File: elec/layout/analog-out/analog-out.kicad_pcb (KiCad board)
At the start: 2 copper layers, 8 parts, among them U1 10kΩ ±1% 62.5mW, U2 10kΩ ±1% 62.5mW, U3 BW CMRR Ib Vos GBW Iout SR, U5 100nF ±10% 50V X7R, U6 100kΩ ±1% 62.5mW, U7 1µF ±10% 25V X5R

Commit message: Build everything with ordered params to fix frozen builds
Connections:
- D1 pad 2: gnd -> gnd-1
- U2 pad 1: gnd -> gnd-1
- U3 pad 4: gnd -> gnd-1
- U3 pad 8: hv -> hv-1
- U4 pad 1: line -> line-1
- U4 pad 2: gnd-1 -> gnd
- U4 pad 3: hv-1 -> hv
- U4 pad 4: line-1 -> line
- U4 pad 6: gnd -> gnd-1
- U5 pad 2: gnd-1 -> gnd
- U6 pad 1: line -> line-1
- U7 pad 1: hv -> hv-1
- U7 pad 2: gnd -> gnd-1
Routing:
- net gnd-1: track 0.00 -> 29.7 mm, vias 0 -> 2
- net gnd: track 29.7 -> 0.00 mm, vias 2 -> 0
- net line-1: track 0.00 -> 1.94 mm
- net line: track 1.94 -> 0.00 mm
- net hv-1: track 0.00 -> 1.56 mm
- net hv: track 1.56 -> 0.00 mm

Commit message: Cleanup layout for usb hub and usb-uart, add CM5 controller heatsink outline
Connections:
- D1 pad 2: gnd-1 -> gnd
- U2 pad 1: gnd-1 -> gnd
- U3 pad 4: gnd-1 -> gnd
- U3 pad 8: hv-1 -> hv
- U4 pad 1: line-1 -> line
- U4 pad 2: gnd -> gnd-1
- U4 pad 3: hv -> hv-1
- U4 pad 4: line -> line-1
- U4 pad 6: gnd-1 -> gnd
- U5 pad 2: gnd -> gnd-1
- U6 pad 1: line-1 -> line
- U7 pad 1: hv-1 -> hv
- U7 pad 2: gnd-1 -> gnd
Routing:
- net gnd-1: track 29.7 -> 0.00 mm, vias 2 -> 0
- net gnd: track 0.00 -> 29.7 mm, vias 0 -> 2
- net line-1: track 1.94 -> 0.00 mm
- net line: track 0.00 -> 1.94 mm
- net hv-1: track 1.56 -> 0.00 mm
- net hv: track 0.00 -> 1.56 mm
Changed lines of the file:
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@@
     )
     (net 0 "")
-    (net 1 "line")
+    (net 1 "line-1")
     (net 2 "amplifier.opamp.footprint.pins[6].net-net")
     (net 3 "amplifier.opamp.footprint.pins[5].net-net")
     (net 4 "non_inverting_input")
     (net 5 "line-2")
-    (net 6 "gnd-1")
-    (net 7 "line-1")
+    (net 6 "gnd")
+    (net 7 "line")
     (net 8 "inverting_input")
     (net 9 "amplifier.opamp.footprint.pins[4].net-net")
-    (net 10 "hv")
+    (net 10 "hv-1")
     (net 11 "output")
-    (net 12 "hv-1")
-    (net 13 "gnd")
+    (net 12 "hv")
+    (net 13 "gnd-1")
     (footprint "atopile:SMB_L4.6-W3.6-LS5.3-RD-330cb3"
         (layer "F.Cu")
@@
             (size 2.05 2.19)
             (layers "F.Cu" "F.Mask" "F.Paste")
-            (net 6 "gnd-1")
+            (net 6 "gnd")
         )
         (embedded_fonts no)
@@
             (size 0.57 0.54)
             (layers "F.Cu" "F.Mask" "F.Paste")
-            (net 7 "line-1")
+            (net 7 "line")
         )
         (pad "2" smd rect
@@
             (size 0.79 0.54)
             (layers "F.Cu" "F.Mask" "F.Paste")
-            (net 12 "hv-1")
+            (net 12 "hv")
         )
         (pad "2" smd rect
@@
             (size 0.79 0.54)
             (layers "F.Cu" "F.Mask" "F.Paste")
-            (net 6 "gnd-1")
+            (net 6 "gnd")
         )
         (embedded_fonts no)
@@
             (size 0.53 1.07)
             (layers "F.Cu" "F.Mask" "F.Paste")
-            (net 7 "line-1")
+            (net 7 "line")
         )
         (pad "2" smd rect
@@
             (size 0.53 1.07)
             (layers "F.Cu" "F.Mask" "F.Paste")
-            (net 13 "gnd")
+            (net 13 "gnd-1")
         )
         (pad "3" smd rect
@@
             (size 0.53 1.07)
             (layers "F.Cu" "F.Mask" "F.Paste")
-            (net 10 "hv")
+            (net 10 "hv-1")
         )
         (pad "4" smd rect
@@
             (size 0.53 1.07)
             (layers "F.Cu" "F.Mask" "F.Paste")
-            (net 1 "line")
+            (net 1 "line-1")
         )
         (pad "5" smd rect
@@
             (size 0.53 1.07)
             (layers "F.Cu" "F.Mask" "F.Paste")
-            (net 6 "gnd-1")
+            (net 6 "gnd")
         )
         (embedded_fonts no)
@@
             (size 0.8 0.9)
             (layers "F.Cu" "F.Mask" "F.Paste")
-            (net 13 "gnd")
+            (net 13 "gnd-1")
         )
         (embedded_fonts no)
@@
             (size 0.57 1.95)
             (layers "F.Cu" "F.Mask" "F.Paste")
-            (net 6 "gnd-1")
+            (net 6 "gnd")
         )
         (pad "5" smd oval
@@
             (size 0.57 1.95)
             (layers "F.Cu" "F.Mask" "F.Paste")
-            (net 12 "hv-1")
+            (net 12 "hv")
         )
         (embedded_fonts no)
@@
             (size 0.57 0.54)
             (layers "F.Cu" "F.Mask" "F.Paste")
-            (net 6 "gnd-1")
+            (net 6 "gnd")
         )
         (pad "2" smd rect

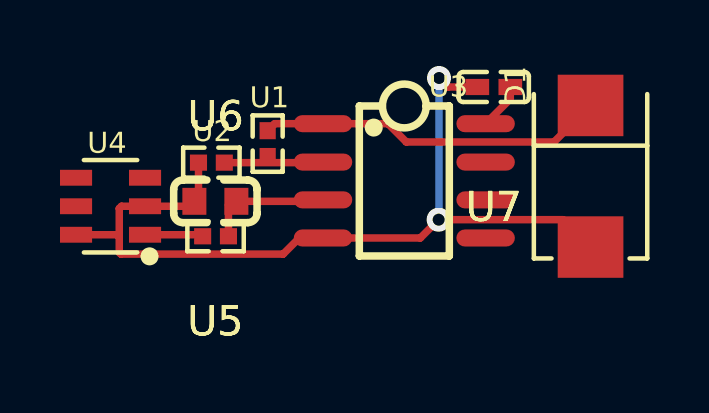
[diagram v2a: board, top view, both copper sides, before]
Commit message: update address pin on analog out, update led value on relay
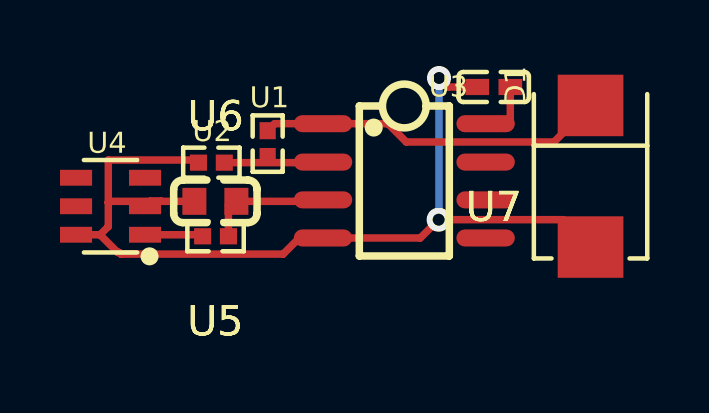
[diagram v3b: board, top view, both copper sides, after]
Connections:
- U4 pad 1: line -> line-1
- U4 pad 2: gnd-1 -> gnd
- U4 pad 4: line-1 -> line-2
- U4 pad 5: line-2 -> line
- U5 pad 2: gnd-1 -> gnd
- U6 pad 1: line -> line-1
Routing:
- net gnd: track 29.7 -> 34.0 mm
- net line-1: track 0.00 -> 1.94 mm
- net line: track 1.94 -> 0.00 mm

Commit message: checkin
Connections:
- U4 pad 4: line-2 -> line
- U4 pad 5: line -> line-2

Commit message: build with excluded checks
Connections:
- U3 pad 8: hv -> hv-1
- U4 pad 1: line-1 -> line-2
- U4 pad 3: hv-1 -> hv
- U4 pad 5: line-2 -> line-1
- U6 pad 1: line-1 -> line-2
- U7 pad 1: hv -> hv-1
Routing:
- net hv-1: track 0.00 -> 2.05 mm
- net hv: track 2.05 -> 0.00 mm
- net line-2: track 0.00 -> 1.94 mm
- net line-1: track 1.94 -> 0.00 mm
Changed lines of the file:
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@@
     (net 3 "amplifier.opamp.footprint.pins[5].net-net")
     (net 4 "non_inverting_input")
-    (net 5 "line-2")
-    (net 6 "line-1")
+    (net 5 "line-1")
+    (net 6 "line-2")
     (net 7 "inverting_input")
     (net 8 "amplifier.opamp.footprint.pins[4].net-net")
-    (net 9 "hv-1")
+    (net 9 "hv")
     (net 10 "output")
-    (net 11 "hv")
+    (net 11 "hv-1")
     (net 12 "gnd")
     (footprint "atopile:SMB_L4.6-W3.6-LS5.3-RD-330cb3"
@@
             (size 0.57 0.54)
             (layers "F.Cu" "F.Mask" "F.Paste")
-            (net 6 "line-1")
+            (net 6 "line-2")
         )
         (pad "2" smd rect
@@
             (size 0.79 0.54)
             (layers "F.Cu" "F.Mask" "F.Paste")
-            (net 11 "hv")
+            (net 11 "hv-1")
         )
         (pad "2" smd rect
@@
             (size 0.53 1.07)
             (layers "F.Cu" "F.Mask" "F.Paste")
-            (net 6 "line-1")
+            (net 6 "line-2")
         )
         (pad "2" smd rect
@@
             (size 0.53 1.07)
             (layers "F.Cu" "F.Mask" "F.Paste")
-            (net 9 "hv-1")
+            (net 9 "hv")
         )
         (pad "4" smd rect
@@
             (size 0.53 1.07)
             (layers "F.Cu" "F.Mask" "F.Paste")
-            (net 5 "line-2")
+            (net 5 "line-1")
         )
         (pad "6" smd rect
@@
             (size 0.57 1.95)
             (layers "F.Cu" "F.Mask" "F.Paste")
-            (net 11 "hv")
+            (net 11 "hv-1")
         )
         (embedded_fonts no)
